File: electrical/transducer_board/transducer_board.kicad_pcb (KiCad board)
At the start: 2 copper layers, 66.6 x 66.6 mm, 65 parts, among them J1 Conn_02x17_Odd_Even, J2 Conn_01x01, J3 Conn_01x01, J4 Conn_01x01, U1 XL62783, U2 XL62083, U3 XL62783, U4 XL62083

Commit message: Tweaks to PCBs
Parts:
- C1, C2, C3, C4, C5, C6, C7, C8: footprint Capacitor_SMD:C_0805_2012Metric -> Capacitor_SMD:C_0603_1608Metric
- moved C8 17.0 mm to (116.8, 132.9)
- moved C6 17.0 mm to (116.8, 135.1)
- moved C7 9.17 mm to (108.7, 116.0)
- moved C5 9.15 mm to (108.7, 118.2)
- moved C1 2.98 mm to (149.8, 132.6)
- moved C4 2.83 mm to (142.2, 153.5)
- moved C2 2.71 mm to (142.2, 151.0)
- moved C3 2.41 mm to (149.8, 135.1)
- moved R11 1.68 mm to (155.3, 146.7)
- moved R23 1.28 mm to (96.6, 138.4)
- moved R31 1.22 mm to (96.6, 146.1)
- moved R3 1.12 mm to (154.7, 138.4)
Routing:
- net VCC: track 173.9 -> 132.1 mm, vias 11 -> 9
- net GND: track 147.5 -> 132.5 mm, vias 6 -> 7
- net /T11-: track 24.9 -> 32.5 mm
- net Net-(LS15-Pad1): track 27.5 -> 20.2 mm
- net Net-(LS7-Pad1): track 30.6 -> 23.9 mm
- net Net-(LS14-Pad1): track 46.1 -> 39.4 mm
- net /T13-: track 16.0 -> 21.9 mm
- net /T10-: track 25.0 -> 30.1 mm
- net /T14-: track 16.8 -> 20.2 mm
- net Net-(R21-Pad2): track 35.7 -> 32.3 mm
- net Net-(LS11-Pad1): track 24.7 -> 21.9 mm
- net Net-(R18-Pad2): track 29.2 -> 26.7 mm
- net Net-(R3-Pad2): track 16.6 -> 14.7 mm
- net Net-(R11-Pad2): track 27.9 -> 26.4 mm
- net Net-(R23-Pad2): track 15.2 -> 14.0 mm
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
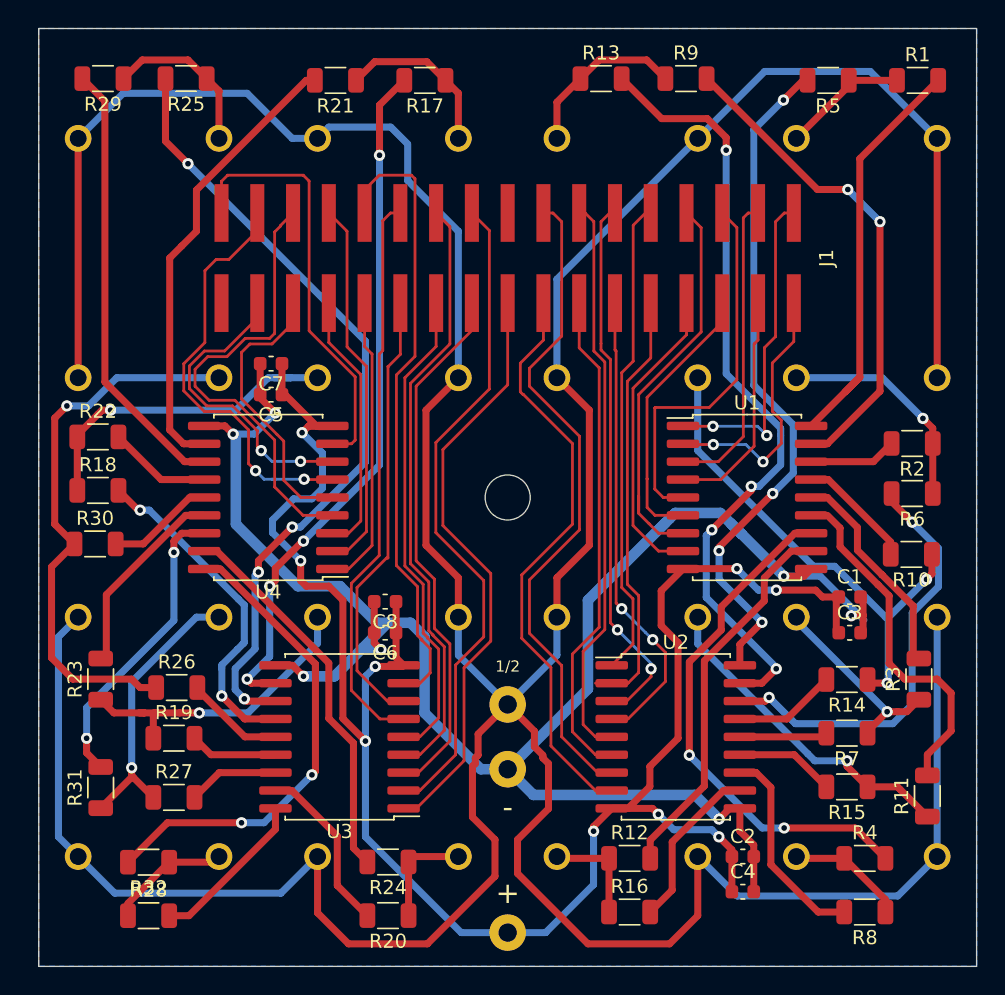
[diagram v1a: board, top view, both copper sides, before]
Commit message: Switched to FPGA on transducer board
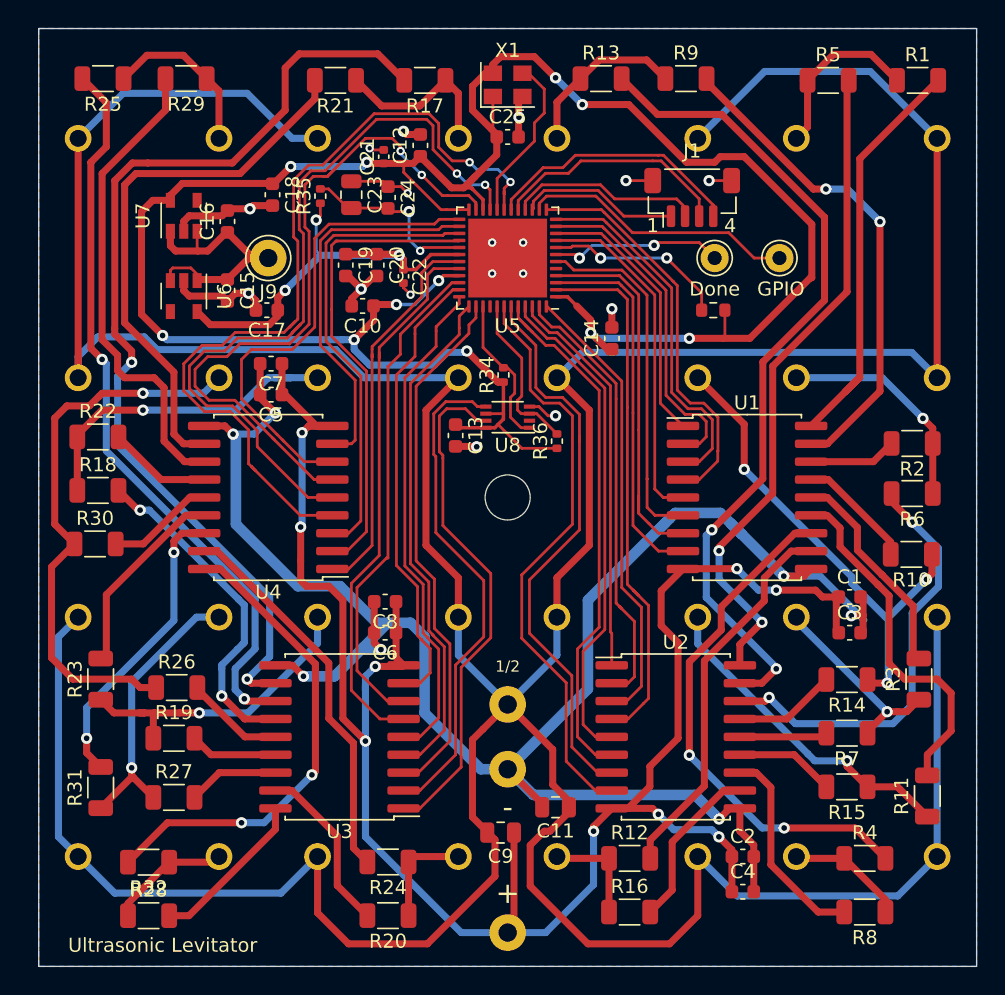
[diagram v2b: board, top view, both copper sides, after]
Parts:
- added C10: 100nF, Capacitor_SMD:C_0603_1608Metric, F.Cu at (115.2, 111.9)
- added C11: 10uF, Capacitor_SMD:C_0805_2012Metric, F.Cu at (128.9, 147.5)
- added C12: 100nF, Capacitor_SMD:C_0603_1608Metric, F.Cu at (119.3, 100.5)
- added C13: 100nF, Capacitor_SMD:C_0603_1608Metric, F.Cu at (121.8, 121.1)
- added C14: 100nF, Capacitor_SMD:C_0603_1608Metric, F.Cu at (132.9, 114.2)
- added C15: 1uF, Capacitor_SMD:C_0603_1608Metric, F.Cu at (105.6, 110.8)
- added C16: 1uF, Capacitor_SMD:C_0603_1608Metric, F.Cu at (105.6, 105.9)
- added C17: 1uF, Capacitor_SMD:C_0603_1608Metric, F.Cu at (108.4, 112.2)
- added C18: 1uF, Capacitor_SMD:C_0603_1608Metric, F.Cu at (108.8, 104.0)
- added C19: 1uF, Capacitor_SMD:C_0603_1608Metric, F.Cu at (114.0, 109.0)
- added C20: 100nF, Capacitor_SMD:C_0603_1608Metric, F.Cu at (116.2, 109.0)
- added C21: 10nF, Capacitor_SMD:C_0402_1005Metric, F.Cu at (116.7, 101.3)
- added C22: 10nF, Capacitor_SMD:C_0402_1005Metric, F.Cu at (118.1, 109.8)
- added C23: 10uF, Capacitor_SMD:C_0805_2012Metric, F.Cu at (114.4, 104.0)
- added C24: 100nF, Capacitor_SMD:C_0603_1608Metric, F.Cu at (117.0, 104.2)
- added C25: 100nF, Capacitor_SMD:C_0603_1608Metric, F.Cu at (125.5, 99.9)
- added C9: 10uF, Capacitor_SMD:C_0805_2012Metric, F.Cu at (125.0, 149.3)
- added J14: Conn_01x01, Connector_Pin:Pin_D1.0mm_L10.0mm, F.Cu at (140.2, 108.5)
- added J6: Conn_01x01, Connector_Pin:Pin_D1.0mm_L10.0mm, F.Cu at (144.8, 108.5)
- added J9: Conn_01x01, Connector_Pin:Pin_D1.3mm_L11.0mm, F.Cu at (108.5, 108.5)
- added R33: 10k, Resistor_SMD:R_0603_1608Metric, F.Cu at (140.1, 112.2)
- added R34: 4.7k, Resistor_SMD:R_0402_1005Metric, F.Cu at (125.2, 116.8)
- added R35: 100, Resistor_SMD:R_0402_1005Metric, F.Cu at (112.2, 104.1)
- added R36: 4.7k, Resistor_SMD:R_0402_1005Metric, F.Cu at (129.0, 121.5)
- added U5: ICE5LP1K-SG48, Package_DFN_QFN:QFN-48-1EP_7x7mm_P0.5mm_EP5.6x5.6mm, F.Cu at (125.5, 108.5)
- added U6: MIC5504-1.2YM5, Package_TO_SOT_SMD:SOT-23-5, F.Cu at (102.5, 111.2)
- added U7: MIC5504-3.3YM5, Package_TO_SOT_SMD:SOT-23-5, F.Cu at (102.5, 105.5)
- added U8: 74LVC3G34, Package_SO:VSSOP-8_2.3x2mm_P0.5mm, F.Cu at (125.5, 119.8)
- added X1: S3D10.000000B20F30T, Oscillator:Oscillator_SMD_Abracon_ASE-4Pin_3.2x2.5mm, F.Cu at (125.5, 96.2)
- C1, C2, C5, C6: value .01uF -> 100nF
- C3, C4, C7, C8: value .1uF -> 1uF
- J1: value Conn_02x17_Odd_Even -> Conn_01x04_MountingPin; footprint Ultrasonic Emitters:PinHeader_2x17_P2.54mm_Vertical_SMD_Wide -> Connector_JST:JST_SH_BM04B-SRSS-TB_1x04-1MP_P1.00mm_Vertical
- R1, R10, R11, R12, R13, R14, R15, R16, R17, R18, R19, R2, R20, R21, R22, R23, R24, R25, R26, R27, R28, R29, R3, R30, R31, R32, R4, R5, R6, R7, R8, R9: value 620 -> 33
- moved J1 13.8 mm to (138.6, 104.2), turned to 0 degrees
- moved R25 5.90 mm to (96.8, 95.8)
- moved R29 5.90 mm to (102.7, 95.8)
- turned R5 to 0 degrees
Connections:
- J1 pad 1: /T1+ -> /SCK
- J1 pad 2: /T5+ -> /SPI_SS
- J1 pad 3: /T2+ -> /SPI_SI
- J1 pad 4: /T6+ -> /SYNC
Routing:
- net /V_3.3: track 0.00 -> 165.7 mm, vias 0 -> 11
- net GND: track 132.5 -> 181.0 mm, vias 7 -> 24
- net /T14-: track 20.2 -> 55.8 mm, vias 0 -> 2
- net /V_1.2: track 0.00 -> 30.9 mm, vias 0 -> 3
- net /T11-: track 32.5 -> 60.7 mm, vias 0 -> 2
- net Net-(R17-Pad2): track 49.3 -> 70.5 mm, vias 4 -> 2
- net /T10-: track 30.1 -> 51.0 mm
- net /V_5: track 0.00 -> 19.9 mm
- net /GPIO_1: track 0.00 -> 19.5 mm
- net /SYNC: track 0.00 -> 18.7 mm
- net /SPI_SI: track 0.00 -> 17.0 mm
- net /T15-: track 18.8 -> 32.9 mm
- net /SPI_SS: track 0.00 -> 13.7 mm
- net /VMID: track 315.2 -> 328.3 mm
- net /CRESET: track 0.00 -> 13.0 mm, vias 0 -> 2
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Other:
- rule via_min_size: 0.4 -> 0.6
- board text added: "1"
- board text added: "4"
- board text added: "Done"
- board text added: "GPIO"
- board text added: "Ultrasonic Levitator"

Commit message: Switched to MachXO3 FPGA
Also switched to Kicad 6
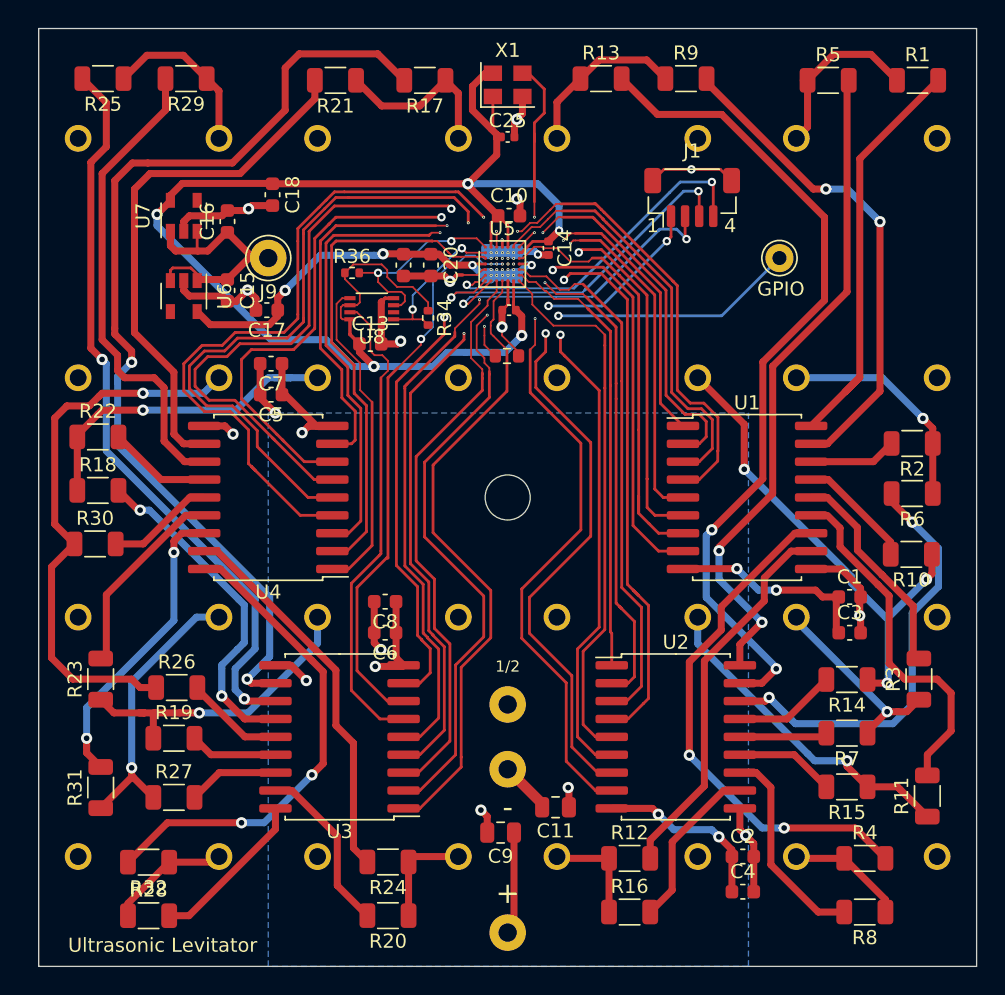
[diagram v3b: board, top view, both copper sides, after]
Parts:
- removed the C21 at (116.7, 101.3)
- removed C23: 10uF, Capacitor_SMD:C_0805_2012Metric
- removed C24: 100nF, Capacitor_SMD:C_0603_1608Metric
- removed J14: Conn_01x01, Connector_Pin:Pin_D1.0mm_L10.0mm
- removed R35: 100, Resistor_SMD:R_0402_1005Metric
- added C22: 1nF, Capacitor_SMD:C_0603_1608Metric_Pad1.08x0.95mm_HandSolder, B.Cu at (126.1, 108.9)
- C12, C14, C25: value 100nF -> 10nF; footprint Capacitor_SMD:C_0603_1608Metric -> Capacitor_SMD:C_0402_1005Metric
- C21: renamed from C22; footprint Capacitor_SMD:C_0402_1005Metric -> Capacitor_SMD:C_0603_1608Metric_Pad1.08x0.95mm_HandSolder; moved to B.Cu
- U5: value ICE5LP1K-SG48 -> LCMXO3L-2100E-5UWG49; footprint Package_DFN_QFN:QFN-48-1EP_7x7mm_P0.5mm_EP5.6x5.6mm -> Package_CSP:ST_WLCSP-49_Die433
- moved R36 18.8 mm to (114.5, 109.5), turned to 0 degrees
- moved R33 15.0 mm to (125.5, 115.5)
- moved C12 13.3 mm to (125.6, 112.2), turned to 180 degrees
- moved U8 12.3 mm to (115.8, 112.1)
- moved C10 12.2 mm to (125.6, 105.5), turned to 0 degrees
- moved C13 8.88 mm to (115.8, 114.6), turned to 0 degrees
- moved C14 7.82 mm to (128.4, 107.8), turned to -90 degrees
- moved R34 6.71 mm to (119.8, 112.8), turned to -90 degrees
- moved C21 6.07 mm to (124.1, 108.9), turned to 90 degrees
- moved C19 4.10 mm to (118.1, 109.0)
- moved C20 3.85 mm to (120.0, 109.0)
- moved U5 0.57 mm to (125.1, 108.9), turned to 0 degrees
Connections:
- R33 pad 1: /CRESET -> /JTAGENB
- R33 pad 2: /V_3.3 -> GND
- R34 pad 2: /T16+_OD -> /T10+_OD
- R36 pad 2: /T12+_OD -> /T16-_OD
- U6 pad 4: Net-(U6-Pad4) -> unconnected-(U6-Pad4)
- U7 pad 4: Net-(U7-Pad4) -> unconnected-(U7-Pad4)
- U8 pad 1: /T16+_OD -> /T10+_OD
- U8 pad 2: Net-(U8-Pad2) -> unconnected-(U8-Pad2)
- U8 pad 3: /T12+_OD -> /T16-_OD
- U8 pad 5: /T12+ -> /T16-
- U8 pad 7: /T16+ -> /T10+
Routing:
- net GND: track 181.0 -> 83.9 mm, vias 24 -> 17
- net VCC: track 135.8 -> 52.0 mm, vias 9 -> 6
- net /V_3.3: track 165.7 -> 110.7 mm, vias 11 -> 5
- net /T16-_OD: track 0.00 -> 14.5 mm, vias 0 -> 2
- net /CRESET: track 13.0 -> 0.00 mm, vias 2 -> 0
- net Net-(C23-Pad2): track 13.0 -> 0.00 mm, vias 2 -> 0
- net /CDONE: track 12.3 -> 0.00 mm, vias 2 -> 0
- net /T12+_OD: track 11.7 -> 0.00 mm
- net /T10+_OD: track 0.00 -> 11.0 mm, vias 0 -> 2
- net /T16+_OD: track 10.7 -> 0.00 mm
- net /T11-: track 60.7 -> 51.3 mm
- net /SPI_SS: track 13.7 -> 22.6 mm, vias 0 -> 2
- net /T16+: track 36.5 -> 45.4 mm
- net /T12+: track 35.5 -> 44.4 mm, vias 0 -> 2
- net /SPI_SI: track 17.0 -> 25.5 mm, vias 0 -> 2
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- added copper zone on In2.Cu, net /VMID
- added copper zone on In1.Cu, net GND
- added copper zone on B.Cu, net VCC
- removed copper zone on B.Cu, net GND
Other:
- copper layers 2 -> 4
- net class Default removed
- board text removed: "Done"

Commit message: Fixed XL62083 pins and made other adjustments
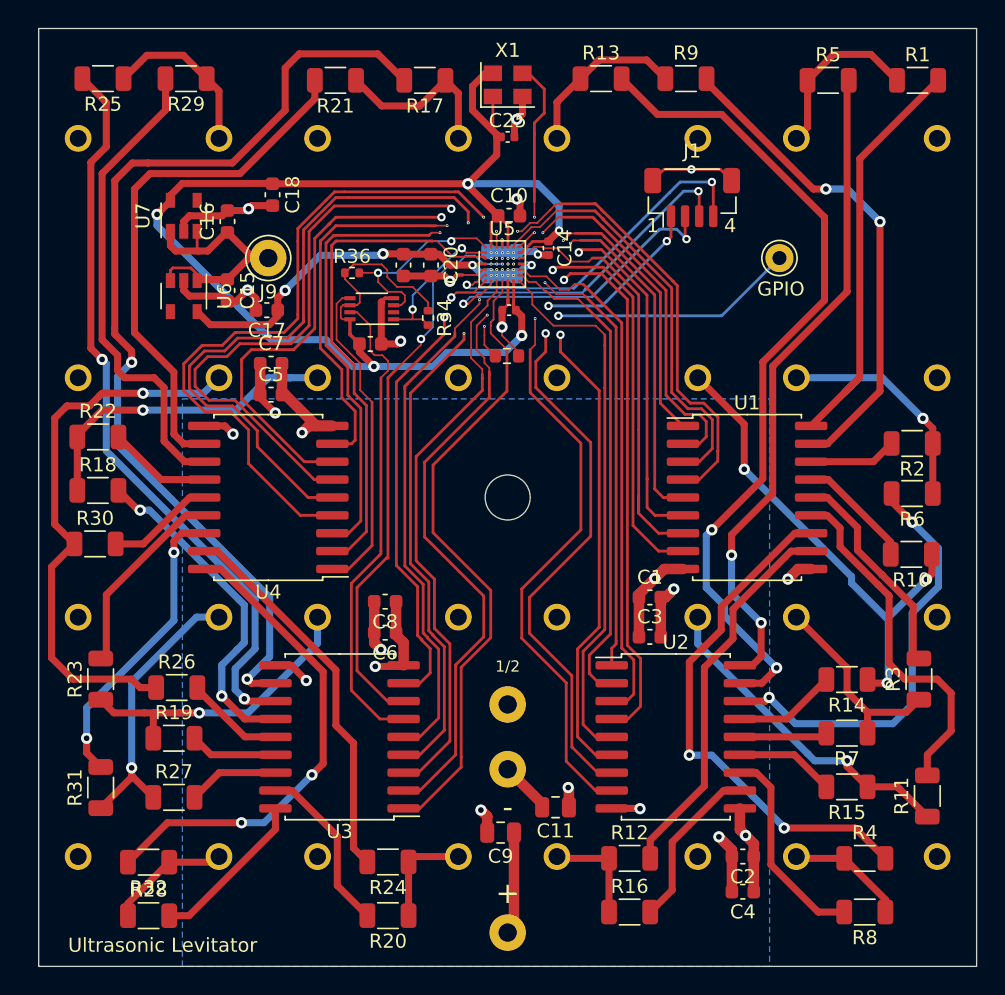
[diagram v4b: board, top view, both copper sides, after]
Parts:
- R1, R10, R11, R12, R13, R14, R15, R16, R17, R18, R19, R2, R20, R21, R22, R23, R24, R25, R26, R27, R28, R29, R3, R30, R31, R32, R4, R5, R6, R7, R8, R9: value 33 -> 50
- moved C3 14.2 mm to (135.6, 135.4)
- moved C1 14.2 mm to (135.6, 132.6)
- turned C2 to 180 degrees
- turned C4 to 180 degrees
- turned C5 to 0 degrees
- turned C7 to 0 degrees
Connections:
- U2 pad 10: GND -> VCC
- U2 pad 9: VCC -> GND
- U4 pad 10: GND -> VCC
- U4 pad 9: VCC -> GND
- U5 pad E6: /T5- -> /T1-
- U5 pad F7: /T1- -> /T5-
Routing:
- net VCC: track 52.0 -> 33.5 mm, vias 6 -> 5
- net GND: track 83.9 -> 85.9 mm, vias 17 -> 18
- net /T5-: track 36.4 -> 34.9 mm, vias 2 -> 0
- net Net-(R4-Pad2): track 38.1 -> 37.0 mm
- net /T1-: track 32.0 -> 33.1 mm, vias 0 -> 2
- net /T6-: track 42.5 -> 41.5 mm
- net Net-(LS3-Pad1): track 14.1 -> 14.7 mm, vias 1 -> 0
- net Net-(R18-Pad2): track 26.7 -> 26.1 mm
- net /T4-: track 44.4 -> 43.9 mm
- net /CLK: track 14.5 -> 14.0 mm

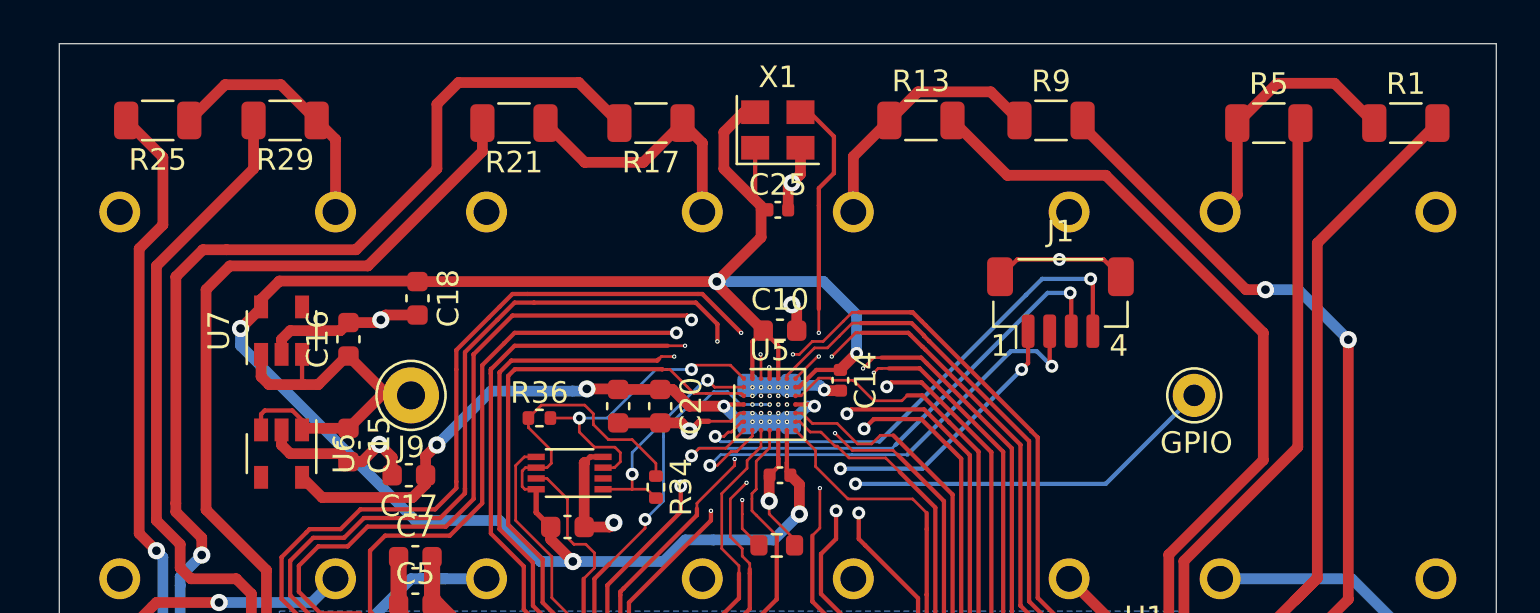
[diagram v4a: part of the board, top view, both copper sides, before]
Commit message: Swapped some parts
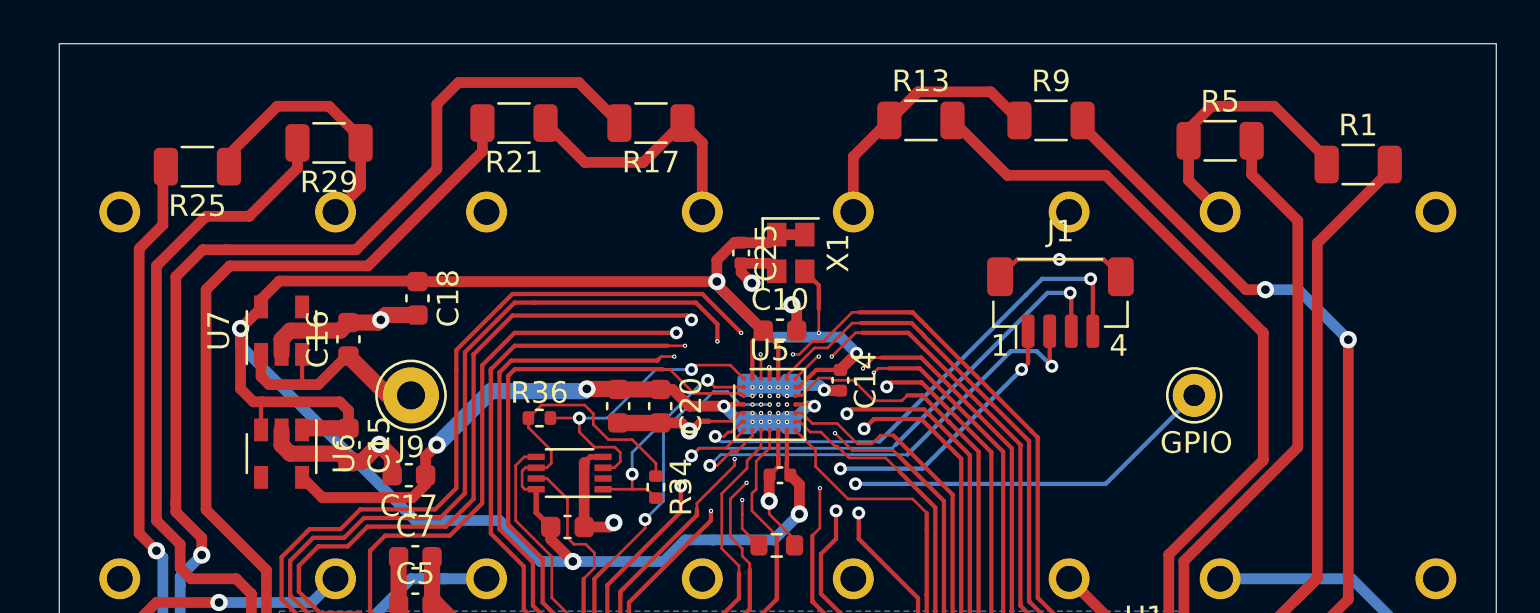
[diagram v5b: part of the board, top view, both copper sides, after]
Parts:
- U6: value MIC5504-1.2YM5 -> ME6211C12M5G-N
- U7: value MIC5504-3.3YM5 -> PJ9193M33SE
- X1: value S3D10.000000B20F30T -> X1G004171001600; footprint Oscillator:Oscillator_SMD_Abracon_ASE-4Pin_3.2x2.5mm -> Oscillator:Oscillator_SMD_SeikoEpson_SG210-4Pin_2.5x2.0mm
- moved X1 5.73 mm to (126.1, 101.9), turned to -90 degrees
- moved R1 2.93 mm to (152.4, 97.8)
- moved R25 2.82 mm to (98.6, 97.9)
- moved C25 2.62 mm to (123.8, 101.9), turned to -90 degrees
- moved R5 2.40 mm to (146.0, 96.7)
- moved R29 2.29 mm to (104.7, 96.8)
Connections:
- C15 pad 1: /V_5 -> /V_3.3
- U6 pad 1: /V_5 -> /V_3.3
- U6 pad 3: /V_5 -> /V_3.3
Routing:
- net /V_5: track 19.9 -> 10.9 mm
- net /CLK: track 14.0 -> 5.72 mm
- net /V_3.3: track 110.5 -> 115.0 mm
- net Net-(R1-Pad2): track 33.2 -> 30.3 mm
- net Net-(R25-Pad2): track 53.2 -> 50.4 mm
- net Net-(R29-Pad2): track 34.1 -> 35.1 mm
